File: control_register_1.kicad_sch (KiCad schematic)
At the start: 6 parts, among them U10 74HC375, U11 74HC02, U12 74HC21, U13 74HC21, U7 74HC04, U9 74HC375

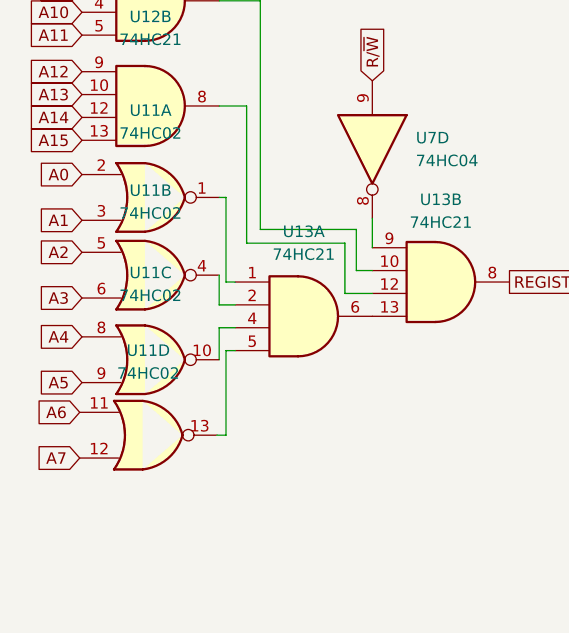
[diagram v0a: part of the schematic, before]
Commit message: add power routing
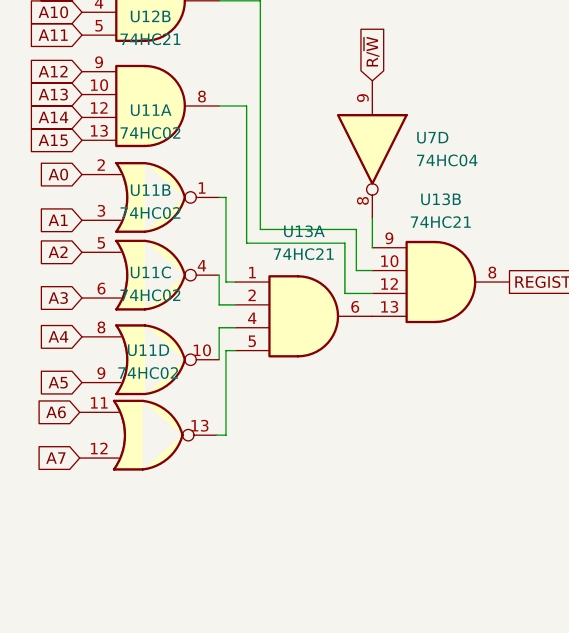
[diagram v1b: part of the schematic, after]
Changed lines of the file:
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@@
     (pin "5")
     (pin "6")
-    (pin "10")
-    (pin "12")
-    (pin "13")
-    (pin "8")
-    (pin "9")
-    (pin "14")
-    (pin "7")
   )
   (symbol (lib_id "74xx:74LS02") (at 53.086 80.264 0) (unit 4)
@@
       (effects (font (size 1.27 1.27)) hide)
     )
-    (pin "1")
-    (pin "2")
-    (pin "3")
-    (pin "4")
-    (pin "5")
-    (pin "6")
-    (pin "10")
-    (pin "8")
-    (pin "9")
     (pin "11")
     (pin "12")
     (pin "13")
-    (pin "14")
-    (pin "7")
   )
   (symbol (lib_id "74xx:74LS02") (at 53.34 62.484 0) (unit 2)
@@
       (effects (font (size 1.27 1.27)) hide)
     )
-    (pin "1")
-    (pin "2")
-    (pin "3")
-    (pin "4")
-    (pin "5")
-    (pin "6")
-    (pin "10")
-    (pin "8")
-    (pin "9")
-    (pin "11")
-    (pin "12")
-    (pin "13")
-    (pin "14")
-    (pin "7")
+    (pin "4")
+    (pin "5")
+    (pin "6")
   )
   (symbol (lib_id "74xx:74LS375") (at 166.878 103.886 0) (unit 1)
@@
       (effects (font (size 1.27 1.27)) hide)
     )
-    (pin "1")
-    (pin "2")
-    (pin "3")
-    (pin "4")
-    (pin "5")
-    (pin "6")
-    (pin "8")
-    (pin "9")
-    (pin "10")
-    (pin "11")
-    (pin "12")
-    (pin "13")
-    (pin "14")
-    (pin "7")
+    (pin "8")
+    (pin "9")
   )
   (symbol (lib_id "74xx:74LS21") (at 53.34 32.004 0) (unit 1)
@@
     (pin "5")
     (pin "6")
-    (pin "10")
-    (pin "12")
-    (pin "13")
-    (pin "8")
-    (pin "9")
-    (pin "14")
-    (pin "7")
   )
   (symbol (lib_id "74xx:74LS02") (at 53.34 71.882 0) (unit 3)
@@
       (effects (font (size 1.27 1.27)) hide)
     )
-    (pin "1")
-    (pin "2")
-    (pin "3")
-    (pin "4")
-    (pin "5")
-    (pin "6")
-    (pin "10")
-    (pin "8")
-    (pin "9")
-    (pin "11")
-    (pin "12")
-    (pin "13")
-    (pin "14")
-    (pin "7")
+    (pin "10")
+    (pin "8")
+    (pin "9")
   )
   (symbol (lib_id "power:+5V") (at 166.878 86.106 0) (unit 1)
@@
     (pin "2")
     (pin "3")
-    (pin "4")
-    (pin "5")
-    (pin "6")
-    (pin "10")
-    (pin "8")
-    (pin "9")
-    (pin "11")
-    (pin "12")
-    (pin "13")
-    (pin "14")
-    (pin "7")
   )
   (symbol (lib_id "74xx:74LS21") (at 53.34 43.688 0) (unit 2)
@@
       (effects (font (size 1.27 1.27)) hide)
     )
-    (pin "1")
-    (pin "2")
-    (pin "4")
-    (pin "5")
-    (pin "6")
-    (pin "10")
-    (pin "12")
-    (pin "13")
-    (pin "8")
-    (pin "9")
-    (pin "14")
-    (pin "7")
+    (pin "10")
+    (pin "12")
+    (pin "13")
+    (pin "8")
+    (pin "9")
   )
   (symbol (lib_id "74xx:74LS21") (at 85.598 63.246 0) (unit 2)
@@
       (effects (font (size 1.27 1.27)) hide)
     )
-    (pin "1")
-    (pin "2")
-    (pin "4")
-    (pin "5")
-    (pin "6")
-    (pin "10")
-    (pin "12")
-    (pin "13")
-    (pin "8")
-    (pin "9")
-    (pin "14")
-    (pin "7")
+    (pin "10")
+    (pin "12")
+    (pin "13")
+    (pin "8")
+    (pin "9")
   )
 )

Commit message: rearrange components for routing
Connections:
- net Q3 renamed P0
- net Q4 renamed P1
- net Q5 renamed P2
- net Q6 renamed P3
- net Q7 renamed P4
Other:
- moved on the sheet: U10, U9

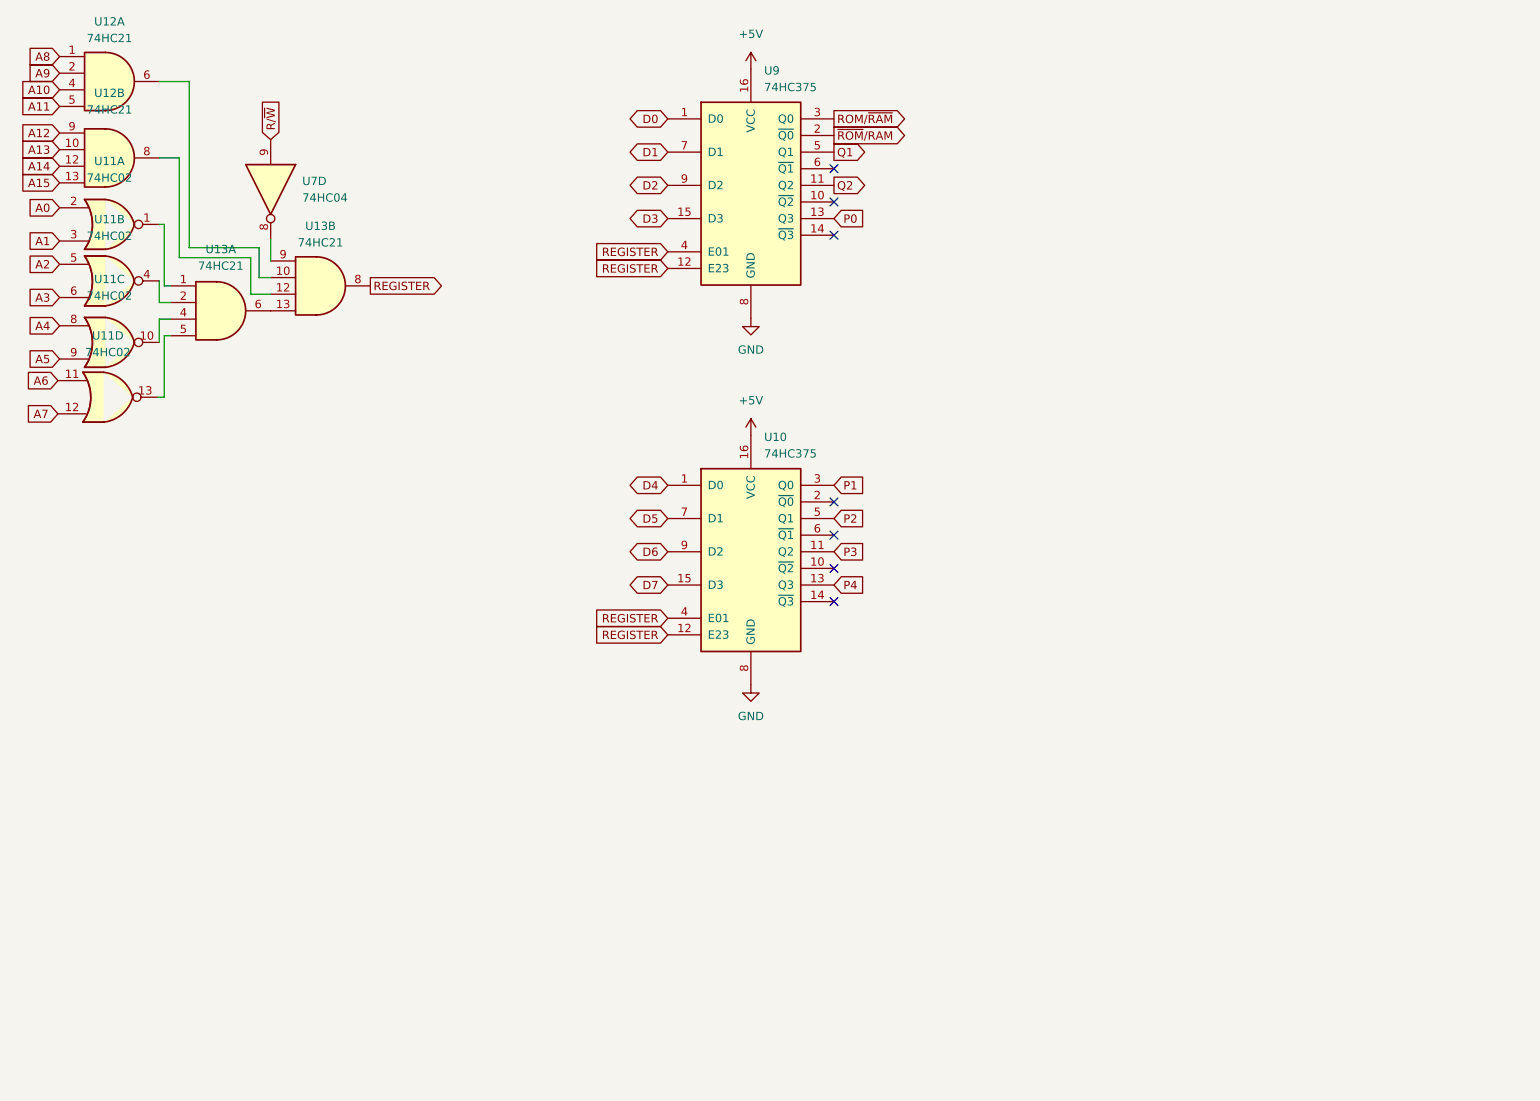
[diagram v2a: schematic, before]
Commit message: reduce component count
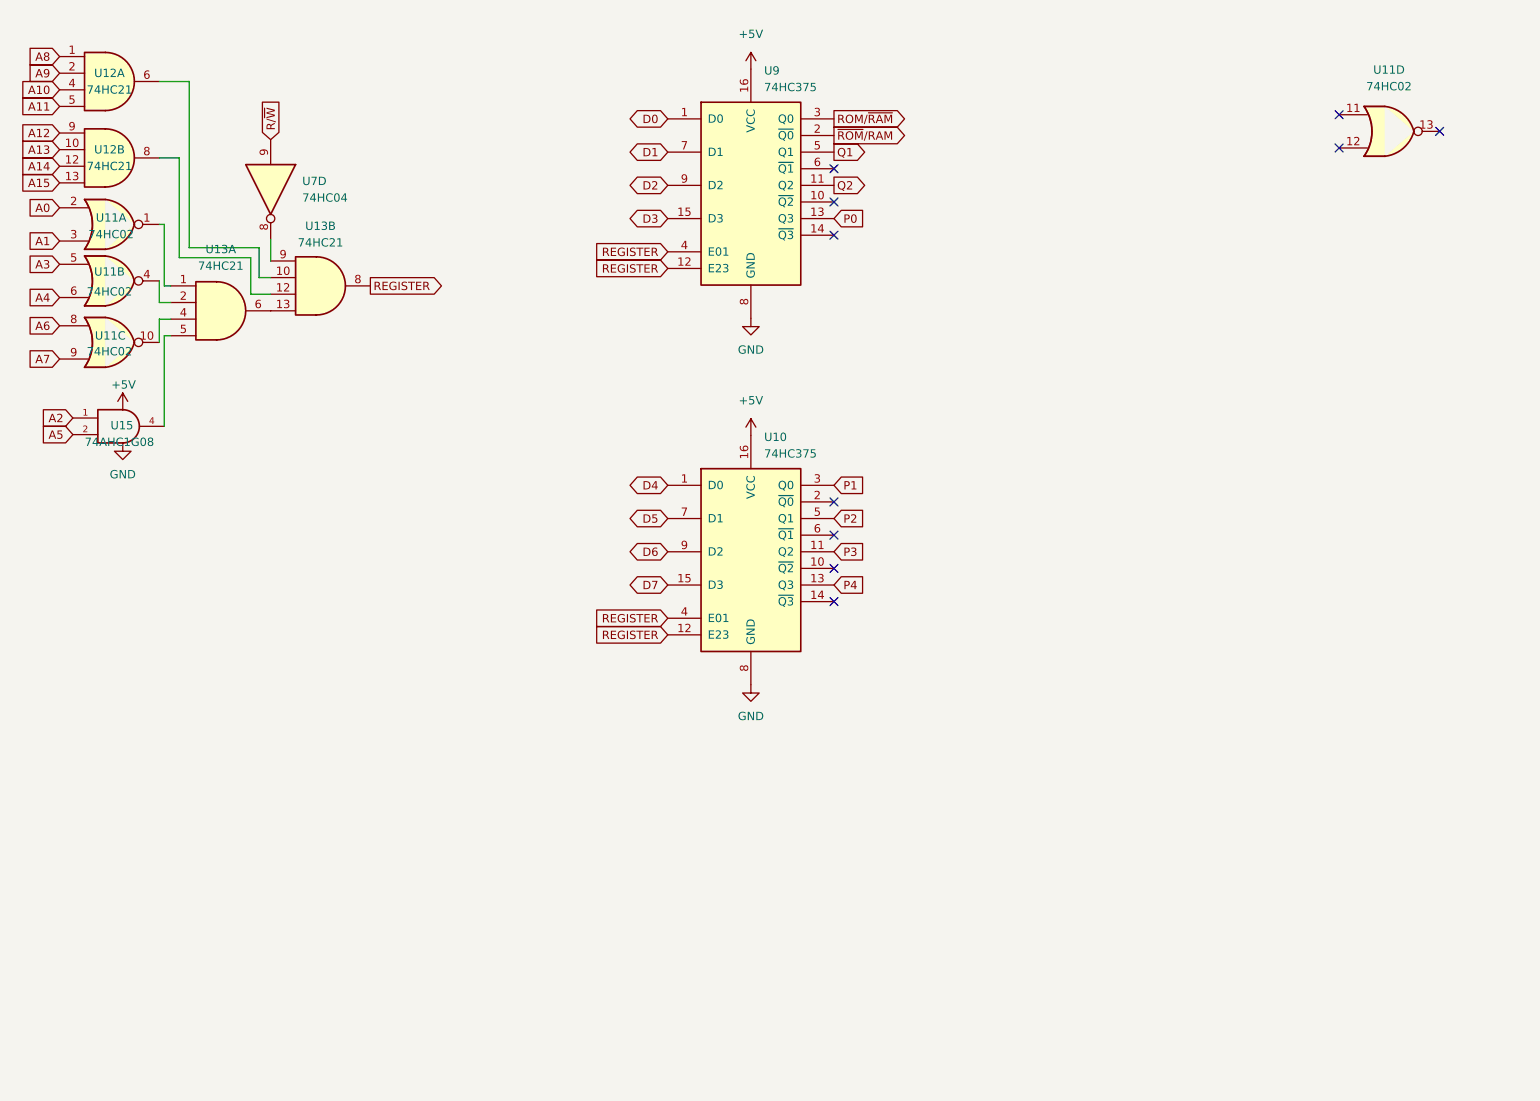
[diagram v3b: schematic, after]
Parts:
- added U15: 74AHC1G08, Package_SO:TSOP-5_1.65x3.05mm_P0.95mm, symbol 74xGxx:74AHC1G08
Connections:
- net +5V: now also U15.5 (VCC)
- net A2: now also U15.1; no longer U11.5
- net A3: now also U11.5; no longer U11.6
- net A4: now also U11.6; no longer U11.8
- net A5: now also U15.2; no longer U11.9
- net A6: now also U11.8; no longer U11.11
- net A7: now also U11.9; no longer U11.12
- net GND: now also U15.3 (GND)
- net at U13.5: now also U15.4; no longer U11.13
- no-connect marks 7 -> 10
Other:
- moved on the sheet: U11D

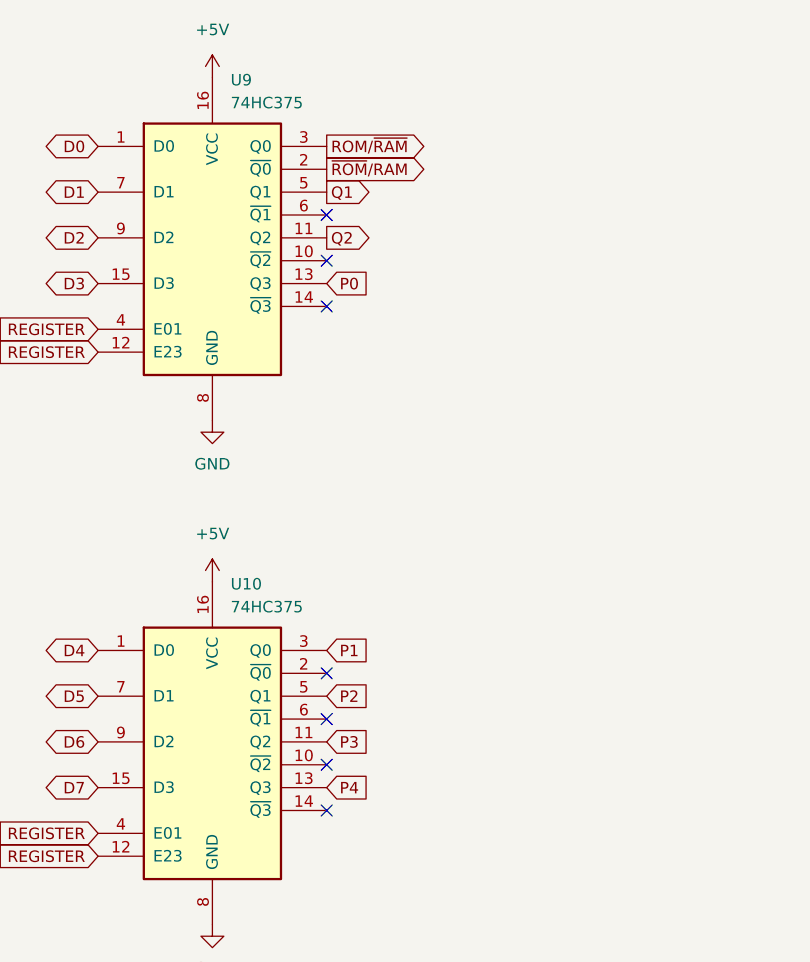
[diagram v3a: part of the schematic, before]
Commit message: correct memory page addressing
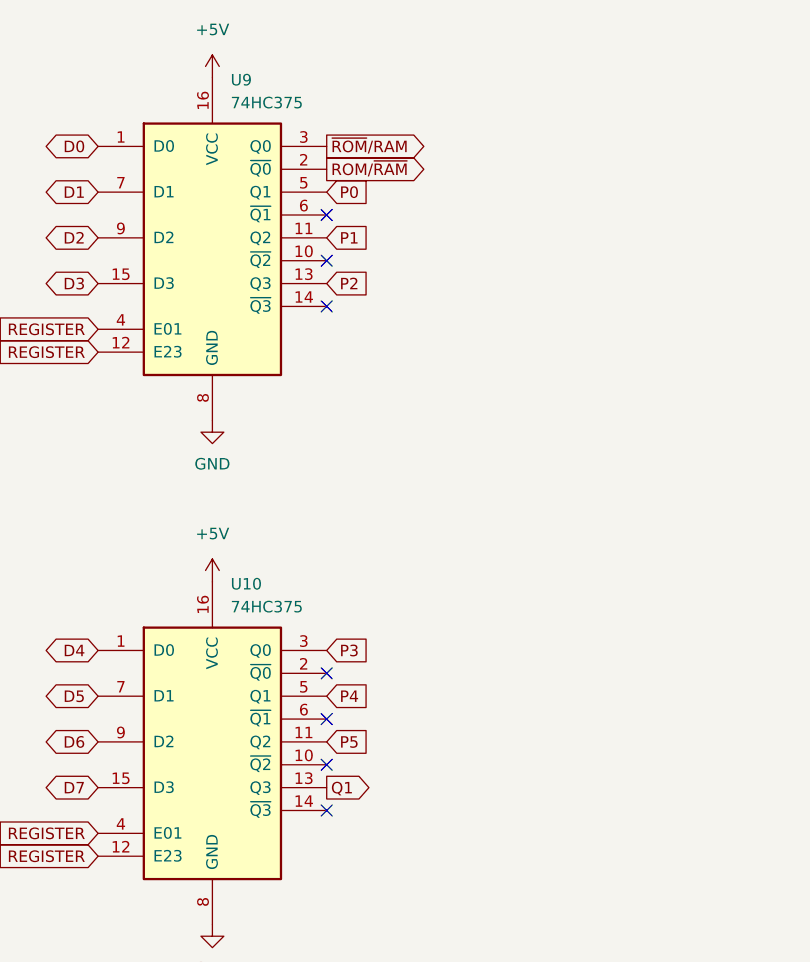
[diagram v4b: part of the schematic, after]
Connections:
- net Q2 is gone; now on net P1: U9.11 (Q2)
- net P0: now also U9.5 (Q1); no longer U9.13 (Q3)
- net P1: no longer U10.3 (Q0)
- net P2: now also U9.13 (Q3); no longer U10.5 (Q1)
- net P3: now also U10.3 (Q0); no longer U10.11 (Q2)
- net P4: now also U10.5 (Q1); no longer U10.13 (Q3)
- net Q1: now also U10.13 (Q3); no longer U9.5 (Q1)
- net ROM/~{RAM}: now also U9.2 (~{Q0}); no longer U9.3 (Q0)
- net ~{ROM}/RAM: now also U9.3 (Q0); no longer U9.2 (~{Q0})
- new net P5: U10.11 (Q2)
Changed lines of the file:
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@@
     )
   )
-  (global_label "P3" (shape input) (at 164.084 103.886 0) (fields_autoplaced)
+  (global_label "P0" (shape input) (at 164.084 42.799 0) (fields_autoplaced)
     (effects (font (size 1.27 1.27)) (justify left))
-    (property "Intersheet References" "${INTERSHEET_REFS}" (id 0) (at 168.9766 103.8066 0)
-      (effects (font (size 1.27 1.27)) (justify left) hide)
-    )
-  )
-  (global_label "P2" (shape input) (at 164.084 98.806 0) (fields_autoplaced)
-    (effects (font (size 1.27 1.27)) (justify left))
-    (property "Intersheet References" "${INTERSHEET_REFS}" (id 0) (at 168.9766 98.7266 0)
+    (property "Intersheet References" "${INTERSHEET_REFS}" (id 0) (at 168.9766 42.7196 0)
       (effects (font (size 1.27 1.27)) (justify left) hide)
     )
@@
     )
   )
-  (global_label "ROM{slash}~{RAM}" (shape output) (at 164.084 37.719 0) (fields_autoplaced)
-    (effects (font (size 1.27 1.27)) (justify left))
-    (property "Intersheet References" "${INTERSHEET_REFS}" (id 0) (at 175.6895 37.6396 0)
-      (effects (font (size 1.27 1.27)) (justify left) hide)
-    )
-  )
   (global_label "A8" (shape input) (at 45.72 28.194 180) (fields_autoplaced)
     (effects (font (size 1.27 1.27)) (justify right))
     (property "Intersheet References" "${INTERSHEET_REFS}" (id 0) (at 41.0088 28.1146 0)
       (effects (font (size 1.27 1.27)) (justify right) hide)
+    )
+  )
+  (global_label "~{ROM}{slash}RAM" (shape output) (at 164.084 37.719 0) (fields_autoplaced)
+    (effects (font (size 1.27 1.27)) (justify left))
+    (property "Intersheet References" "${INTERSHEET_REFS}" (id 0) (at 175.6895 37.7984 0)
+      (effects (font (size 1.27 1.27)) (justify left) hide)
     )
   )
@@
     )
   )
+  (global_label "Q1" (shape output) (at 164.084 108.966 0) (fields_autoplaced)
+    (effects (font (size 1.27 1.27)) (justify left))
+    (property "Intersheet References" "${INTERSHEET_REFS}" (id 0) (at 169.0371 109.0454 0)
+      (effects (font (size 1.27 1.27)) (justify left) hide)
+    )
+  )
   (global_label "A6" (shape input) (at 45.72 69.342 180) (fields_autoplaced)
     (effects (font (size 1.27 1.27)) (justify right))
     (property "Intersheet References" "${INTERSHEET_REFS}" (id 0) (at 41.0088 69.2626 0)
       (effects (font (size 1.27 1.27)) (justify right) hide)
-    )
-  )
-  (global_label "P1" (shape input) (at 164.084 93.726 0) (fields_autoplaced)
-    (effects (font (size 1.27 1.27)) (justify left))
-    (property "Intersheet References" "${INTERSHEET_REFS}" (id 0) (at 168.9766 93.6466 0)
-      (effects (font (size 1.27 1.27)) (justify left) hide)
     )
   )
@@
     )
   )
+  (global_label "P3" (shape input) (at 164.084 93.726 0) (fields_autoplaced)
+    (effects (font (size 1.27 1.27)) (justify left))
+    (property "Intersheet References" "${INTERSHEET_REFS}" (id 0) (at 168.9766 93.6466 0)
+      (effects (font (size 1.27 1.27)) (justify left) hide)
+    )
+  )
   (global_label "A14" (shape input) (at 45.72 44.958 180) (fields_autoplaced)
     (effects (font (size 1.27 1.27)) (justify right))
@@
     (property "Intersheet References" "${INTERSHEET_REFS}" (id 0) (at 41.0088 64.9446 0)
       (effects (font (size 1.27 1.27)) (justify right) hide)
-    )
-  )
-  (global_label "Q1" (shape output) (at 164.084 42.799 0) (fields_autoplaced)
-    (effects (font (size 1.27 1.27)) (justify left))
-    (property "Intersheet References" "${INTERSHEET_REFS}" (id 0) (at 169.0371 42.8784 0)
-      (effects (font (size 1.27 1.27)) (justify left) hide)
     )
   )
@@
     )
   )
+  (global_label "P4" (shape input) (at 164.084 98.806 0) (fields_autoplaced)
+    (effects (font (size 1.27 1.27)) (justify left))
+    (property "Intersheet References" "${INTERSHEET_REFS}" (id 0) (at 168.9766 98.7266 0)
+      (effects (font (size 1.27 1.27)) (justify left) hide)
+    )
+  )
   (global_label "D2" (shape bidirectional) (at 138.684 47.879 180) (fields_autoplaced)
     (effects (font (size 1.27 1.27)) (justify right))
@@
     )
   )
+  (global_label "P1" (shape input) (at 164.084 47.879 0) (fields_autoplaced)
+    (effects (font (size 1.27 1.27)) (justify left))
+    (property "Intersheet References" "${INTERSHEET_REFS}" (id 0) (at 168.9766 47.7996 0)
+      (effects (font (size 1.27 1.27)) (justify left) hide)
+    )
+  )
   (global_label "A15" (shape input) (at 45.72 47.498 180) (fields_autoplaced)
     (effects (font (size 1.27 1.27)) (justify right))
@@
     )
   )
-  (global_label "P0" (shape input) (at 164.084 52.959 0) (fields_autoplaced)
+  (global_label "P2" (shape input) (at 164.084 52.959 0) (fields_autoplaced)
     (effects (font (size 1.27 1.27)) (justify left))
     (property "Intersheet References" "${INTERSHEET_REFS}" (id 0) (at 168.9766 52.8796 0)
@@
     )
   )
-  (global_label "Q2" (shape output) (at 164.084 47.879 0) (fields_autoplaced)
+  (global_label "ROM{slash}~{RAM}" (shape output) (at 164.084 40.259 0) (fields_autoplaced)
     (effects (font (size 1.27 1.27)) (justify left))
-    (property "Intersheet References" "${INTERSHEET_REFS}" (id 0) (at 169.0371 47.7996 0)
+    (property "Intersheet References" "${INTERSHEET_REFS}" (id 0) (at 175.6895 40.3384 0)
       (effects (font (size 1.27 1.27)) (justify left) hide)
     )
   )
-  (global_label "~{ROM}{slash}RAM" (shape output) (at 164.084 40.259 0) (fields_autoplaced)
+  (global_label "P5" (shape input) (at 164.084 103.886 0) (fields_autoplaced)
     (effects (font (size 1.27 1.27)) (justify left))
-    (property "Intersheet References" "${INTERSHEET_REFS}" (id 0) (at 175.6895 40.1796 0)
+    (property "Intersheet References" "${INTERSHEET_REFS}" (id 0) (at 168.9766 103.8066 0)
       (effects (font (size 1.27 1.27)) (justify left) hide)
     )
@@
     )
   )
-  (global_label "P4" (shape input) (at 164.084 108.966 0) (fields_autoplaced)
-    (effects (font (size 1.27 1.27)) (justify left))
-    (property "Intersheet References" "${INTERSHEET_REFS}" (id 0) (at 168.9766 108.8866 0)
-      (effects (font (size 1.27 1.27)) (justify left) hide)
-    )
-  )
